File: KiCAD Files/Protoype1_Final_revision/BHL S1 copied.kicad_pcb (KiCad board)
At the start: 4 copper layers, 64 x 64 mm, 106 parts, among them IC1 NUP2105LT1G, IC2 NUP2105LT1G, IC4 FD6288Q, J1 39-30-1042, J2 Conn_01x03_Pin, J3 Conn_01x03_Pin, J4 39-30-1042, Q1 CSD19502Q5B, Q2 CSD19502Q5B, Q3 CSD19502Q5B, Q4 CSD19502Q5B, Q5 CSD19502Q5B, Q7 CSD19502Q5B, U1 ME6211C30M5, U2 SPX3819M5-L-5-0, U3 Solder Pad, U5 STM32G431CBU6, Y1 8MHz

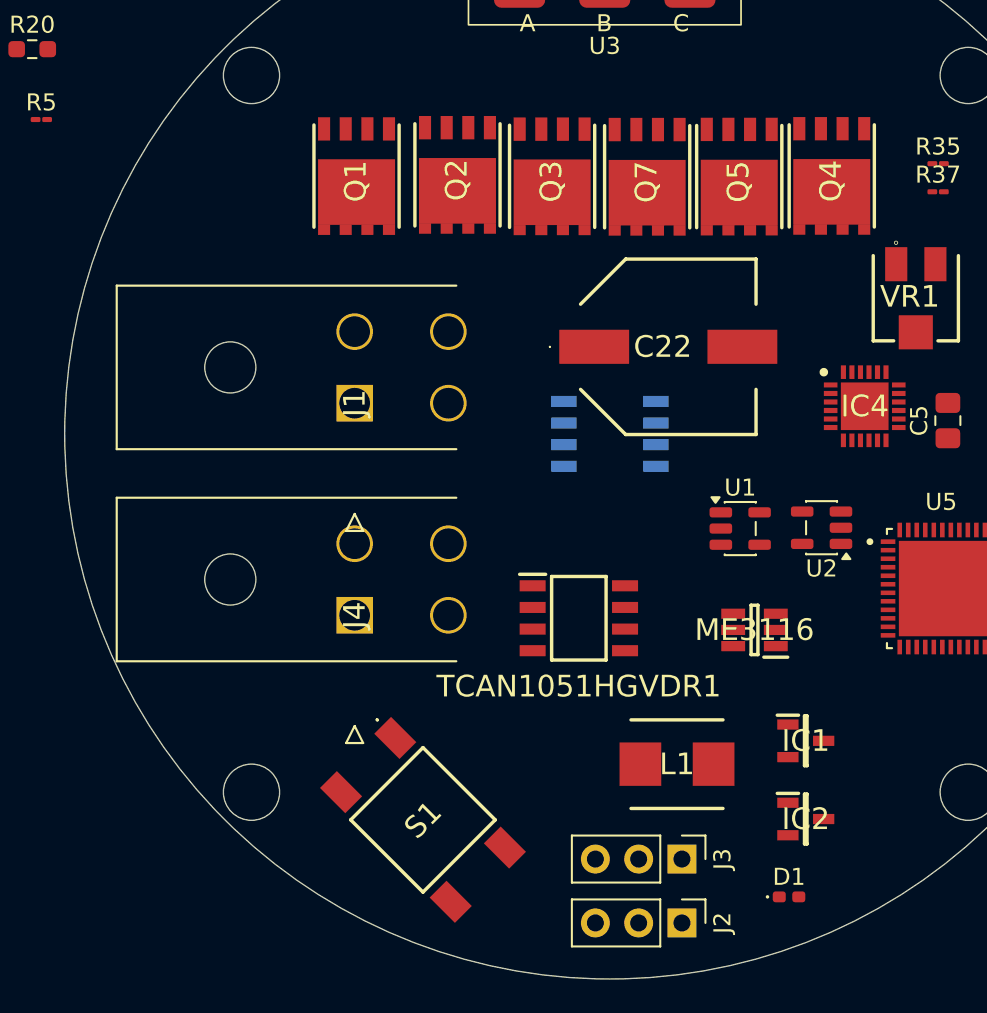
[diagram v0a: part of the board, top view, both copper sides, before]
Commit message: fixed some errors
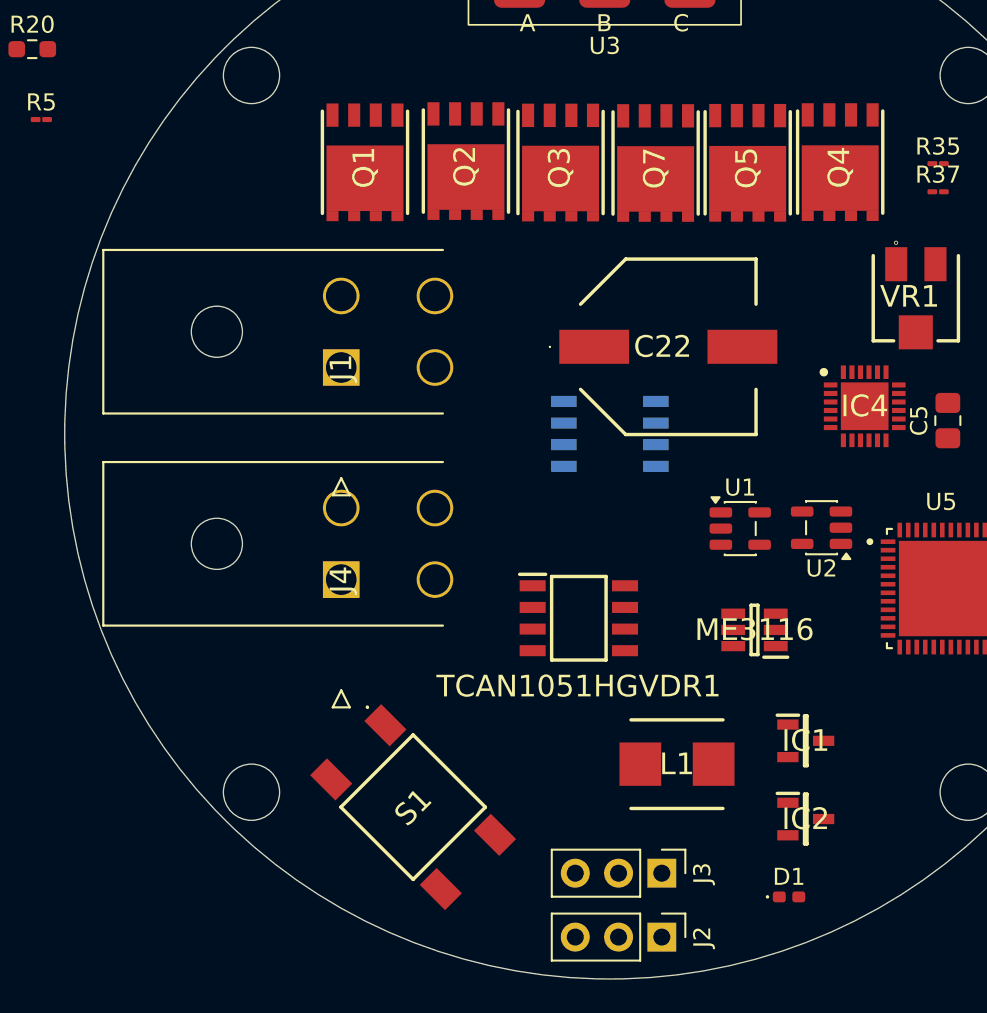
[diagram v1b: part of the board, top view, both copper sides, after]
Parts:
- moved J1 2.24 mm to (182.0, 79.6)
- moved J4 2.24 mm to (182.0, 92.0)
- moved J2 1.44 mm to (200.8, 113.0)
- moved J3 1.44 mm to (200.8, 109.2)
- moved Q1 0.95 mm to (183.4, 67.5)
- moved Q2 0.95 mm to (189.3, 67.4)
- moved Q3 0.95 mm to (194.8, 67.5)
- moved Q4 0.95 mm to (211.3, 67.5)
- moved Q5 0.95 mm to (205.8, 67.5)
- moved Q7 0.95 mm to (200.4, 67.6)
- moved S1 0.94 mm to (186.2, 105.4)
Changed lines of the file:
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@@
 		)
 		(embedded_fonts no)
-		(model "C:/Users/jiaxi/Downloads/LIB_EEE-FN1V471UP/EEE-FN1V471UP/3D/EEE-FN1V471UP.stp"
+		(model "/Users/elijahrobinson/Documents/GitHub/Robot-Dog/KiCAD Files/3D models/EEE-FN1V471UP_ECAP.stp"
 			(offset
 				(xyz 0 0 1)
@@
 	(footprint "Connector_PinHeader_2.54mm:PinHeader_1x03_P2.54mm_Vertical"
 		(layer "F.Cu")
-		(at 201.97 112.17 -90)
+		(at 200.79 113 -90)
 		(descr "Through hole straight pin header, 1x03, 2.54mm pitch, single row")
 		(tags "Through hole pin header THT 1x03 2.54mm single row")
@@
 		)
 		(embedded_fonts no)
-		(model "C:/Users/jiaxi/Downloads/LIB_0530CDMCCDS-6R8MC/0530CDMCCDS-6R8MC/3D/0530CDMCCDS-6R8MC.stp"
+		(model "/Users/elijahrobinson/Documents/GitHub/Robot-Dog/KiCAD Files/3D models/0530CDMCCDS-6R8MC_Inductor.stp"
 			(offset
 				(xyz 0 0 0)
@@
 	(footprint "Footprint for BHL S1:CSD19502Q5B_MOSFET"
 		(layer "F.Cu")
-		(at 205.335 68.359 90)
+		(at 205.83 67.55 90)
 		(descr "Q5B")
 		(tags "MOSFET (P-Channel)")
@@
 		)
 		(embedded_fonts no)
-		(model "C:/Users/jiaxi/Downloads/LIB_CSD19502Q5B/CSD19502Q5B/3D/CSD19502Q5B.stp"
+		(model "/Users/elijahrobinson/Documents/GitHub/Robot-Dog/KiCAD Files/3D models/CSD19502Q5B_MOS.stp"
 			(offset
 				(xyz 0 0 0)
@@
 		)
 		(embedded_fonts no)
-		(model "C:/Users/jiaxi/Documents/GitHub/Quadraped-Robot/KiCAD Files/3D models/FD6288Q_GateDRIVER.stp"
+		(model "/Users/elijahrobinson/Documents/GitHub/Robot-Dog/KiCAD Files/3D models/FD6288Q_GateDRIVER.stp"
 			(offset
 				(xyz 0 0 0)
@@
 	(footprint "Footprint for BHL S1:CSD19502Q5B_MOSFET"
 		(layer "F.Cu")
-		(at 188.795 68.258 90)
+		(at 189.29 67.449 90)
 		(descr "Q5B")
 		(tags "MOSFET (P-Channel)")
@@
 		)
 		(embedded_fonts no)
-		(model "C:/Users/jiaxi/Downloads/LIB_CSD19502Q5B/CSD19502Q5B/3D/CSD19502Q5B.stp"
+		(model "/Users/elijahrobinson/Documents/GitHub/Robot-Dog/KiCAD Files/3D models/CSD19502Q5B_MOS.stp"
 			(offset
 				(xyz 0 0 0)
@@
 	(footprint "Footprint for BHL S1:Terminator"
 		(layer "F.Cu")
-		(at 182.76 81.66 -90)
+		(at 181.9719 79.56575 -90)
 		(descr "39-30-104Y")
 		(tags "Connector")
@@
 		)
 		(embedded_fonts no)
-		(model "C:/Users/jiaxi/Downloads/LIB_39-30-1042/39-30-1042/3D/39-30-1042.stp"
+		(model "/Users/elijahrobinson/Documents/GitHub/Robot-Dog/KiCAD Files/3D models/39-30-1042_Terminal.stp"
 			(offset
 				(xyz -2 -14 0)
@@
 	(footprint "Footprint for BHL S1:CSD19502Q5B_MOSFET"
 		(layer "F.Cu")
-		(at 182.87 68.329 90)
+		(at 183.365 67.52 90)
 		(descr "Q5B")
 		(tags "MOSFET (P-Channel)")
@@
 		)
 		(embedded_fonts no)
-		(model "C:/Users/jiaxi/Downloads/LIB_CSD19502Q5B/CSD19502Q5B/3D/CSD19502Q5B.stp"
+		(model "/Users/elijahrobinson/Documents/GitHub/Robot-Dog/KiCAD Files/3D models/CSD19502Q5B_MOS.stp"
 			(offset
 				(xyz 0 0 0)
@@
 		)
 		(embedded_fonts no)
-		(model "C:/Users/jiaxi/Downloads/LIB_NUP2105LT1G/NUP2105LT1G/3D/NUP2105LT1G.stp"
+		(model "/Users/elijahrobinson/Documents/GitHub/Robot-Dog/KiCAD Files/3D models/NUP2105LT1G_DIODIDE.stp"
 			(offset
 				(xyz 0 0 0)
@@
 	(footprint "Footprint for BHL S1:CSD19502Q5B_MOSFET"
 		(layer "F.Cu")
-		(at 199.93 68.369 90)
+		(at 200.425 67.56 90)
 		(descr "Q5B")
 		(tags "MOSFET (P-Channel)")
@@
 		)
 		(embedded_fonts no)
-		(model "C:/Users/jiaxi/Downloads/LIB_CSD19502Q5B/CSD19502Q5B/3D/CSD19502Q5B.stp"
+		(model "/Users/elijahrobinson/Documents/GitHub/Robot-Dog/KiCAD Files/3D models/CSD19502Q5B_MOS.stp"
 			(offset
 				(xyz 0 0 0)
@@
 	(footprint "Footprint for BHL S1:Push Button 6x6mm"
 		(layer "F.Cu")
-		(at 186.77 106.12 45)
+		(at 186.191674 105.373654 45)
 		(descr "1571563-6-2")
 		(tags "Switch (4-Pin Push)")
@@
 		)
 		(embedded_fonts no)
-		(model "C:/Users/jiaxi/Downloads/LIB_1571563-6/1571563-6/3D/Small_pushbutton_pad.stp"
+		(model "/Users/elijahrobinson/Documents/GitHub/Robot-Dog/KiCAD Files/3D models/Small_pushbutton_pad.stp"
 			(offset
 				(xyz 0 0 0)
@@
 		)
 		(embedded_fonts no)
-		(model "C:/Users/jiaxi/Documents/GitHub/Quadraped-Robot/KiCAD Files/3D models/STM32G431CBU6.step"
+		(model "/Users/elijahrobinson/Documents/GitHub/Robot-Dog/KiCAD Files/3D models/STM32G431CBU6_Newlyuploadedby_JJ.stp"
 			(offset
 				(xyz 0 0 0)
@@
 		)
 		(embedded_fonts no)
-		(model "C:/Users/jiaxi/Downloads/LIB_TCAN1051HGVDR/TCAN1051HGVDR/3D/TCAN1051HGVDR.stp"
+		(model "/Users/elijahrobinson/Documents/GitHub/Robot-Dog/KiCAD Files/3D models/TCAN1051HGVDR_CAN.stp"
 			(offset
 				(xyz 0 0 0)
@@
 		)
 		(embedded_fonts no)
-		(model "C:/Users/jiaxi/Downloads/LIB_3314J-1-103G/3314J-1-103G/3D/3314J-1-103G.stp"
+		(model "/Users/elijahrobinson/Documents/GitHub/Robot-Dog/KiCAD Files/3D models/3314J-1-103G_Trimerpot_Forthermal.stp"
 			(offset
 				(xyz 0 0 0)
@@
 	(footprint "Connector_PinHeader_2.54mm:PinHeader_1x03_P2.54mm_Vertical"
 		(layer "F.Cu")
-		(at 201.97 108.42 -90)
+		(at 200.79 109.25 -90)
 		(descr "Through hole straight pin header, 1x03, 2.54mm pitch, single row")
 		(tags "Through hole pin header THT 1x03 2.54mm single row")
@@
 	(footprint "Footprint for BHL S1:Terminator"
 		(layer "F.Cu")
-		(at 182.76 94.11 -90)
+		(at 181.9719 92.01575 -90)
 		(descr "39-30-104Y")
 		(tags "Connector")
@@
 		)
 		(embedded_fonts no)
-		(model "C:/Users/jiaxi/Downloads/LIB_39-30-1042/39-30-1042/3D/39-30-1042.stp"
+		(model "/Users/elijahrobinson/Documents/GitHub/Robot-Dog/KiCAD Files/3D models/39-30-1042_Terminal.stp"
 			(offset
 				(xyz -2 -14 0)
@@
 		)
 		(embedded_fonts no)
-		(model "C:/Users/jiaxi/Downloads/LIB_NUP2105LT1G/NUP2105LT1G/3D/NUP2105LT1G.stp"
+		(model "/Users/elijahrobinson/Documents/GitHub/Robot-Dog/KiCAD Files/3D models/NUP2105LT1G_DIODIDE.stp"
 			(offset
 				(xyz 0 0 0)
@@
 	(footprint "Footprint for BHL S1:CSD19502Q5B_MOSFET"
 		(layer "F.Cu")
-		(at 194.35 68.343 90)
+		(at 194.845 67.534 90)
 		(descr "Q5B")
 		(tags "MOSFET (P-Channel)")
@@
 		)
 		(embedded_fonts no)
-		(model "C:/Users/jiaxi/Downloads/LIB_CSD19502Q5B/CSD19502Q5B/3D/CSD19502Q5B.stp"
+		(model "/Users/elijahrobinson/Documents/GitHub/Robot-Dog/KiCAD Files/3D models/CSD19502Q5B_MOS.stp"
 			(offset
 				(xyz 0 0 0)
@@
 		)
 		(embedded_fonts no)
-		(model "C:/Users/jiaxi/Downloads/LIB_CSTNE8M00G55Z000R0/CSTNE8M00G55Z000R0/3D/CSTNE8M00G55Z000R0.stp"
+		(model "/Users/elijahrobinson/Documents/GitHub/Robot-Dog/KiCAD Files/3D models/CSTNE8M00G55Z000R0_Resonator.stp"
 			(offset
 				(xyz 0 0 0)
@@
 	(footprint "Footprint for BHL S1:CSD19502Q5B_MOSFET"
 		(layer "F.Cu")
-		(at 210.765 68.319 90)
+		(at 211.26 67.51 90)
 		(descr "Q5B")
 		(tags "MOSFET (P-Channel)")
@@
 		)
 		(embedded_fonts no)
-		(model "C:/Users/jiaxi/Downloads/LIB_CSD19502Q5B/CSD19502Q5B/3D/CSD19502Q5B.stp"
+		(model "/Users/elijahrobinson/Documents/GitHub/Robot-Dog/KiCAD Files/3D models/CSD19502Q5B_MOS.stp"
 			(offset
 				(xyz 0 0 0)
@@
 		)
 		(embedded_fonts no)
-		(model "C:/Users/jiaxi/Downloads/LIB_AS5600-ASOT/AS5600-ASOT/3D/AS5600-ASOT.stp"
+		(model "/Users/elijahrobinson/Documents/GitHub/Robot-Dog/KiCAD Files/3D models/AS5600-ASOT.stp"
 			(offset
 				(xyz 0 0 0)

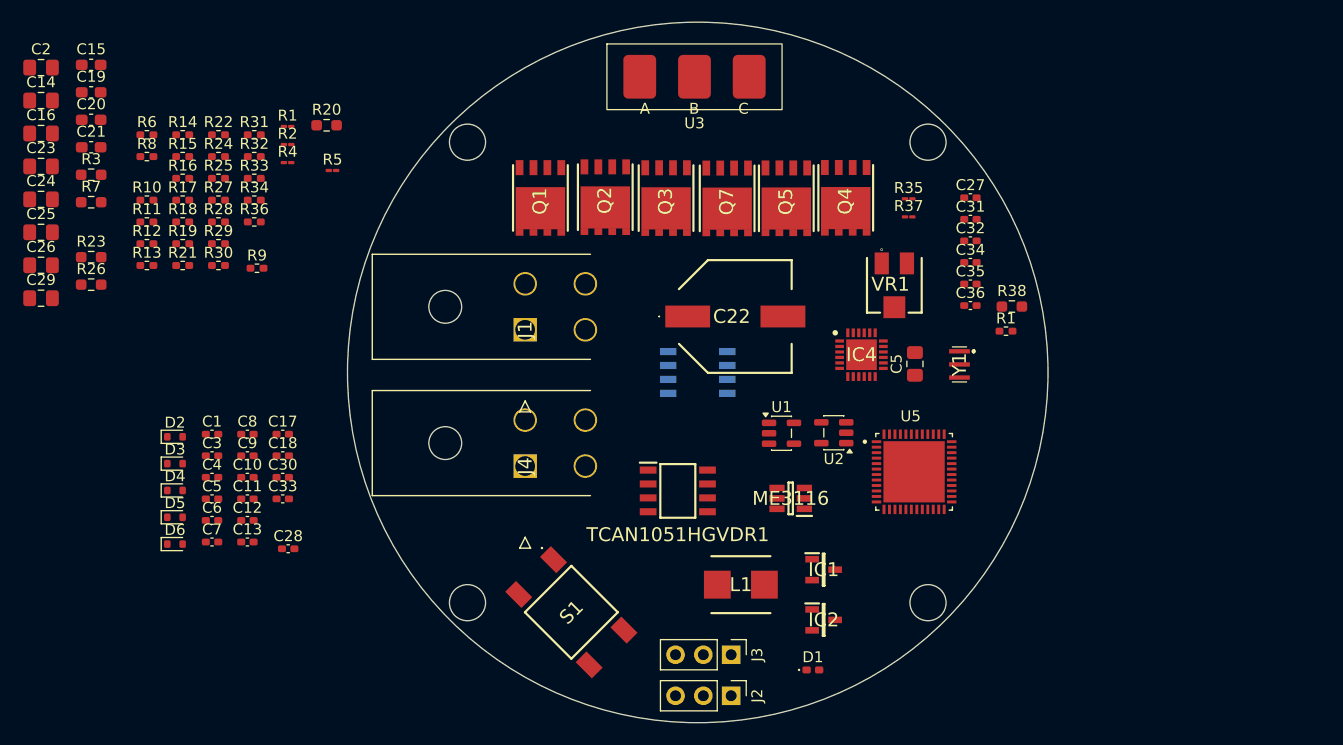
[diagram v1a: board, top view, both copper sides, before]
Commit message: Fixed all Errors in Schematic and Started routing PCB traces
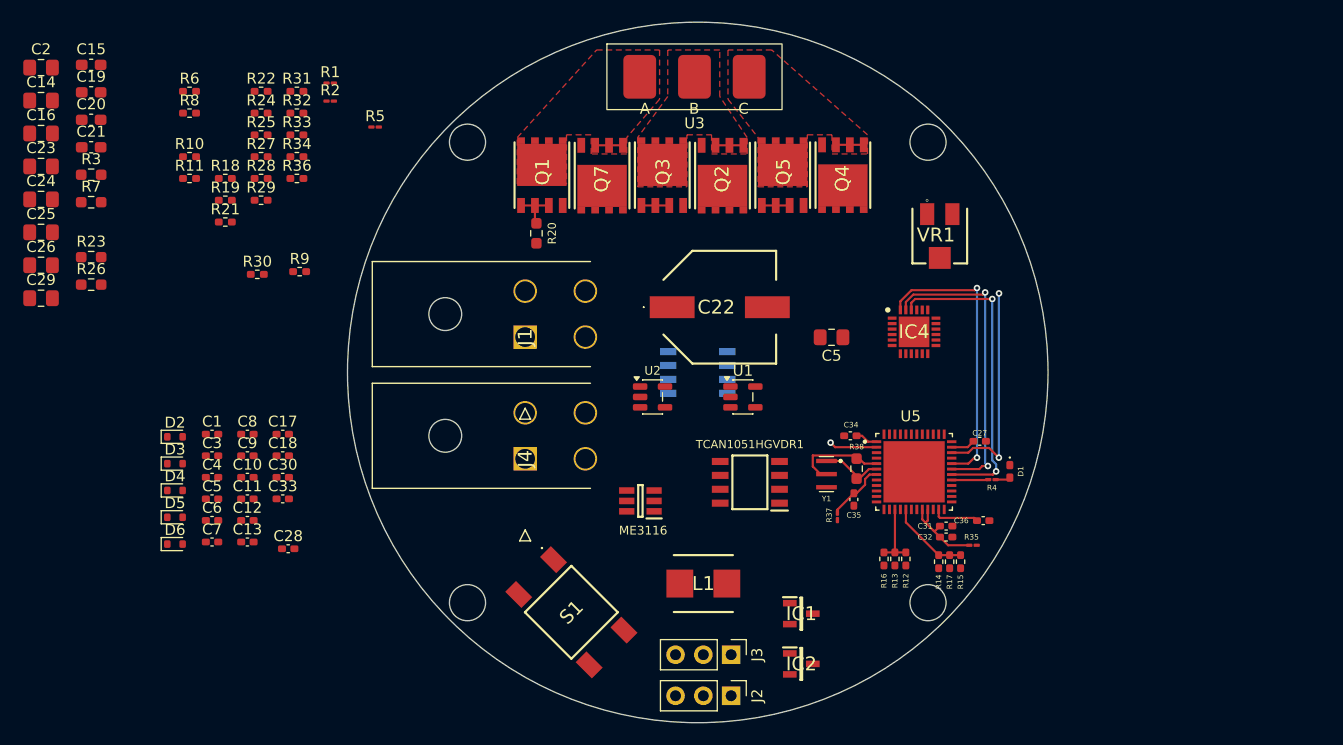
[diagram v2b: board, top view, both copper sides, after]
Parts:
- removed the R1 at (225.9, 79.7)
- moved R15 80.1 mm to (221.8, 100.8), turned to -90 degrees
- moved R14 79.3 mm to (219.8, 100.8), turned to -90 degrees
- moved R17 77.5 mm to (220.8, 100.8), turned to 90 degrees
- moved R12 75.1 mm to (216.8, 100.5), turned to -90 degrees
- moved R16 73.8 mm to (215.8, 100.5), turned to 90 degrees
- moved R13 72.5 mm to (214.8, 100.5), turned to -90 degrees
- moved R4 70.6 mm to (224.6, 93.2), turned to 180 degrees
- moved R35 32.2 mm to (222.9, 99.2)
- moved R37 28.1 mm to (210.5, 96.6), turned to 90 degrees
- moved C31 28.1 mm to (220.4, 97.5)
- moved C32 27.2 mm to (220.4, 98.5)
- moved D1 25.5 mm to (226.2, 92.5), turned to -90 degrees
- moved C35 22.4 mm to (212.0, 95.1), turned to 90 degrees
- moved C27 22.3 mm to (223.5, 89.8)
- moved R20 21.6 mm to (183.0, 70.8), turned to -90 degrees
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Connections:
- net VCC_5V_CAN renamed Net-(TCAN1051HGVDR1-VIO)
- AS5600 pad 1: +3.3V -> VCC_5V
- AS5600 pad 8: +3.3V -> VCC_5V
- C28 pad 1: +3.3V -> VCC_5V
- C3 pad 1: +3.3V -> VCC_5V
- C33 pad 1: +3.3V -> VCC_5V
- C4 pad 1: +3.3V -> VCC_5V
- J1 pad 4: VCC_IN_22V -> DCBUS
- J2 pad 1: SWCLK -> GND
- J2 pad 2: GND -> SWCLK
- R29 pad 1: +3.3V -> VCC_5V
- R33 pad 2: +3.3V -> VCC_5V
- R34 pad 2: +3.3V -> VCC_5V
- TCAN1051HGVDR1 pad 3: +3.3V -> VCC_5V
- U1 pad 1: +3.3V -> VCC_5V
- U1 pad 3: +3.3V -> VCC_5V
- U2 pad 5: +3.3V -> VCC_5V
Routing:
- net HIN1: track 0.00 -> 28.3 mm, vias 0 -> 2
- net HIN2: track 0.00 -> 27.7 mm, vias 0 -> 2
- net HIN3: track 0.00 -> 26.3 mm, vias 0 -> 2
- net LIN2: track 0.00 -> 19.9 mm, vias 0 -> 2
- net Net-(U5-PF0-OSC_IN): track 0.00 -> 9.22 mm
- net +3.3V: track 0.00 -> 8.57 mm
- net Net-(U5-VDDA): track 0.00 -> 8.23 mm
- net Curr_fdbk3_OPAmp+: track 0.00 -> 7.42 mm
- net Curr_fdbk2_OPAmp+: track 0.00 -> 5.93 mm
- net Net-(U5-PF1-OSC_OUT): track 0.00 -> 5.60 mm
- net Net-(U5-PG10-~{RST}): track 0.00 -> 5.48 mm
- net LIN1: track 0.00 -> 4.37 mm, vias 0 -> 1
- net Vshunt_1+: track 0.00 -> 4.33 mm
- net STATUS: track 0.00 -> 3.35 mm
- net Vshunt_3+: track 0.00 -> 2.54 mm
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- added copper zone on In1.Cu, net GND
- added copper zone on F.Cu, net SH_A
- added copper zone on F.Cu, net SH_B
- added copper zone on F.Cu, net SH_C

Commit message: PCB layout changes
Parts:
- removed R28: 0, Resistor_SMD:R_0402_1005Metric_Pad0.72x0.64mm_HandSolder
- moved R27 67.7 mm to (225.5, 64.0)
- moved R26 62.9 mm to (205.0, 70.8), turned to -90 degrees
- moved C21 62.1 mm to (204.4, 61.0)
- moved R24 51.8 mm to (208.5, 70.5), turned to -90 degrees
- moved R23 51.5 mm to (193.8, 70.8), turned to 90 degrees
- moved C20 51.1 mm to (193.4, 60.8)
- moved R25 50.4 mm to (207.5, 70.5), turned to -90 degrees
- moved R21 42.7 mm to (197.2, 70.5), turned to -90 degrees
- moved R22 40.5 mm to (196.2, 70.5), turned to -90 degrees
- moved C19 40.0 mm to (182.2, 60.8)
- moved R18 32.3 mm to (186.5, 70.5), turned to -90 degrees
- moved R19 31.0 mm to (185.5, 70.5), turned to -90 degrees
- moved C22 2.02 mm to (198.0, 78.5)
- moved U1 1.95 mm to (203.5, 86.8)
- moved U2 1.95 mm to (195.2, 86.8)
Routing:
- net SH_A: track 2.54 -> 20.3 mm
- net SH_C: track 2.54 -> 18.9 mm
- net SH_B: track 2.54 -> 18.5 mm
- net Net-(Q4-G): track 0.00 -> 7.69 mm
- net Net-(Q7-G): track 0.00 -> 7.65 mm
- net Net-(Q2-G): track 0.00 -> 7.54 mm
- net Net-(Q3-G): track 0.00 -> 1.76 mm
- net Net-(Q5-G): track 0.00 -> 1.74 mm
- net Net-(Q1-G): track 0.00 -> 1.74 mm
- net Vshunt_3+: track 2.54 -> 4.23 mm
- net Vshunt_2+: track 2.54 -> 4.22 mm
- removed copper zone on F.Cu, net SH_A
- removed copper zone on F.Cu, net SH_B
- removed copper zone on F.Cu, net SH_C

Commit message: worked on PCB routing
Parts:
- R38: footprint Resistor_SMD:R_0603_1608Metric_Pad0.98x0.95mm_HandSolder -> Resistor_SMD:R_0402_1005Metric_Pad0.72x0.64mm_HandSolder
- moved Y1 13.9 mm to (222.7, 97.1), turned to -135 degrees
- moved C36 11.9 mm to (212.6, 101.0)
- moved R35 10.4 mm to (212.5, 100.0)
- moved R38 9.21 mm to (220.6, 96.2), turned to 45 degrees
- moved C31 9.06 mm to (212.6, 102.0)
- moved C32 9.06 mm to (212.6, 103.0)
- moved R14 1.75 mm to (218.0, 100.8)
- moved R15 1.75 mm to (220.0, 100.8)
- moved R17 1.75 mm to (219.0, 100.8)
- moved C28 0.81 mm to (159.8, 99.0)
- turned IC4 to 135 degrees
- turned U5 to 135 degrees
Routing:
- net HIN1: track 28.3 -> 0.00 mm, vias 2 -> 0
- net HIN2: track 27.7 -> 0.00 mm, vias 2 -> 0
- net HIN3: track 26.3 -> 0.00 mm, vias 2 -> 0
- net LIN2: track 19.9 -> 0.00 mm, vias 2 -> 0
- net +3.3V: track 8.57 -> 0.00 mm
- net Net-(U5-VDDA): track 8.23 -> 0.00 mm
- net Curr_fdbk3_OPAmp+: track 7.42 -> 2.00 mm
- net Net-(U5-PG10-~{RST}): track 5.48 -> 0.28 mm
- net LIN1: track 4.37 -> 0.00 mm, vias 1 -> 0
- net Curr_fdbk2_OPAmp+: track 5.93 -> 2.01 mm
- net STATUS: track 3.35 -> 0.06 mm
- net GND: track 0.00 -> 1.77 mm, vias 0 -> 1
- net Net-(U5-PF1-OSC_OUT): track 5.60 -> 4.38 mm
- net Net-(D1-A): track 1.37 -> 0.25 mm
- net Net-(U5-PF0-OSC_IN): track 9.22 -> 8.68 mm
